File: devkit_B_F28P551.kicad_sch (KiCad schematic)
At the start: 4 parts, among them J1 DEVKIT_C2000_ROW_A, J2 DEVKIT_C2000_ROW_B, J3 JTAG_CTBP_10, U1 TMS320F28P551SG5PM

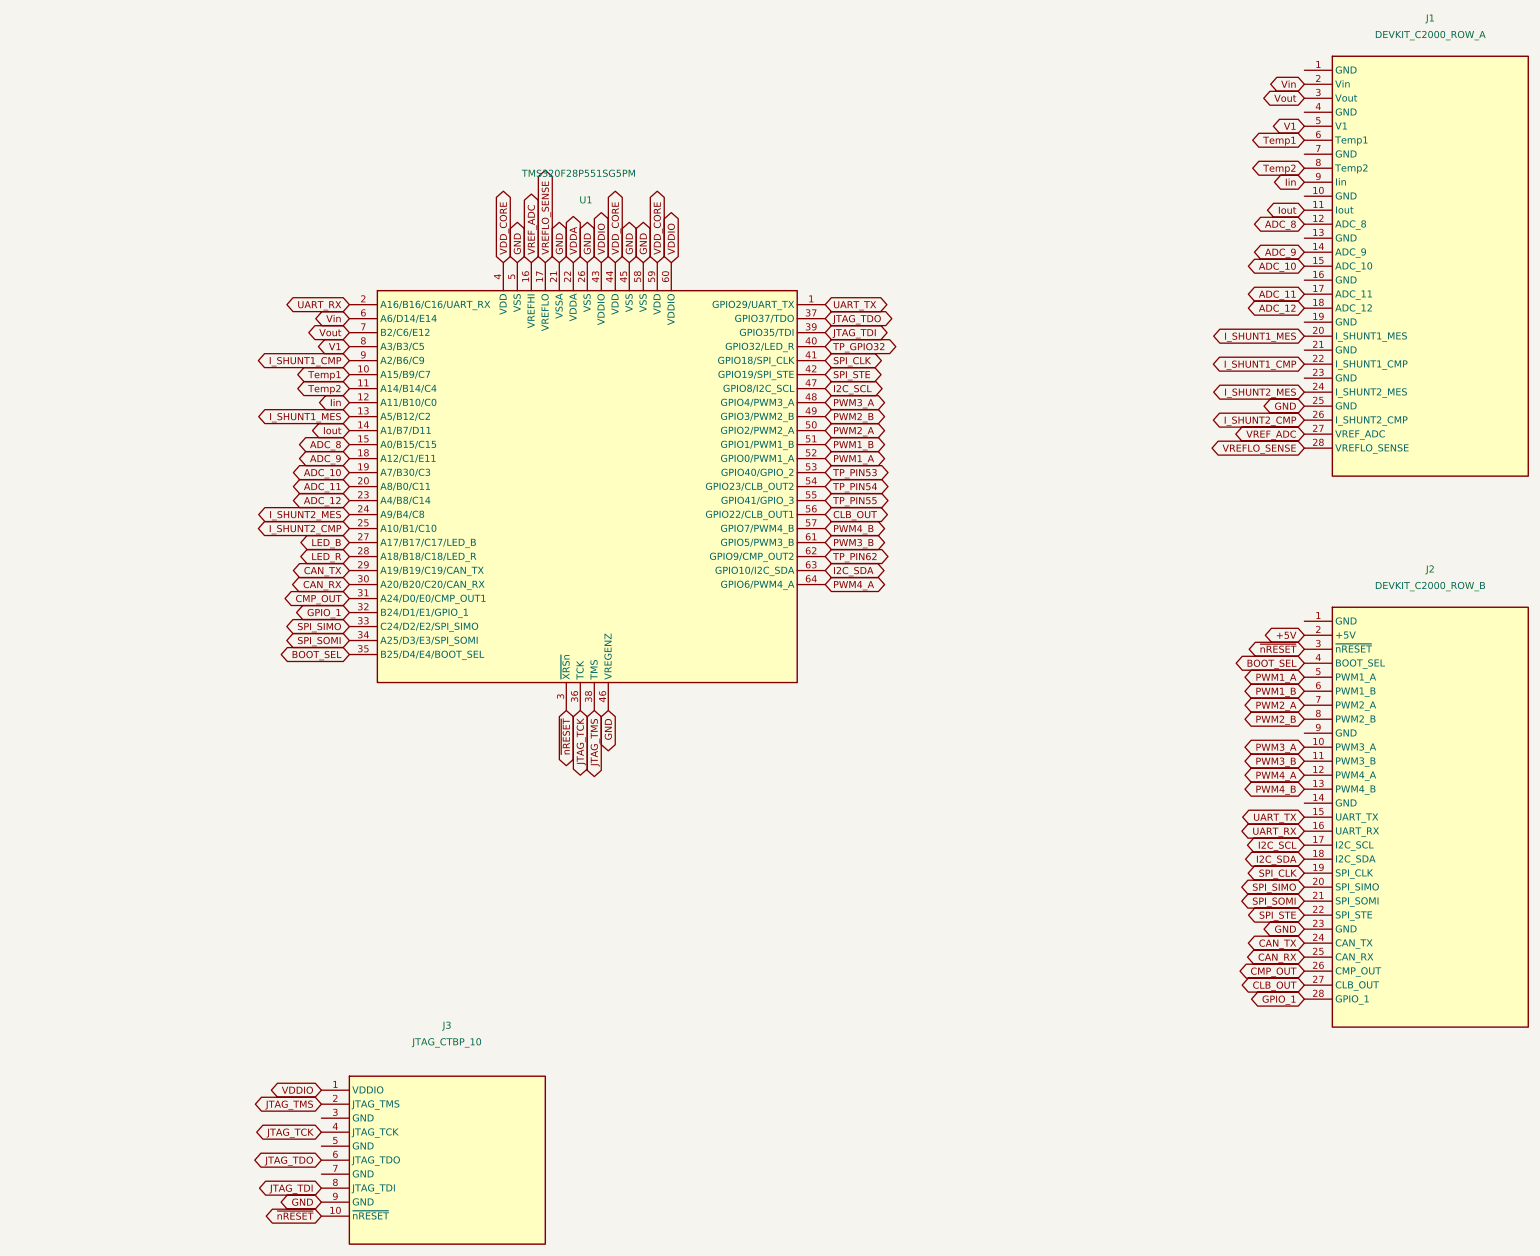
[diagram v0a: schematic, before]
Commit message: Symboles MCU en carre LQFP-64, 16 broches par cote de 1 a 64
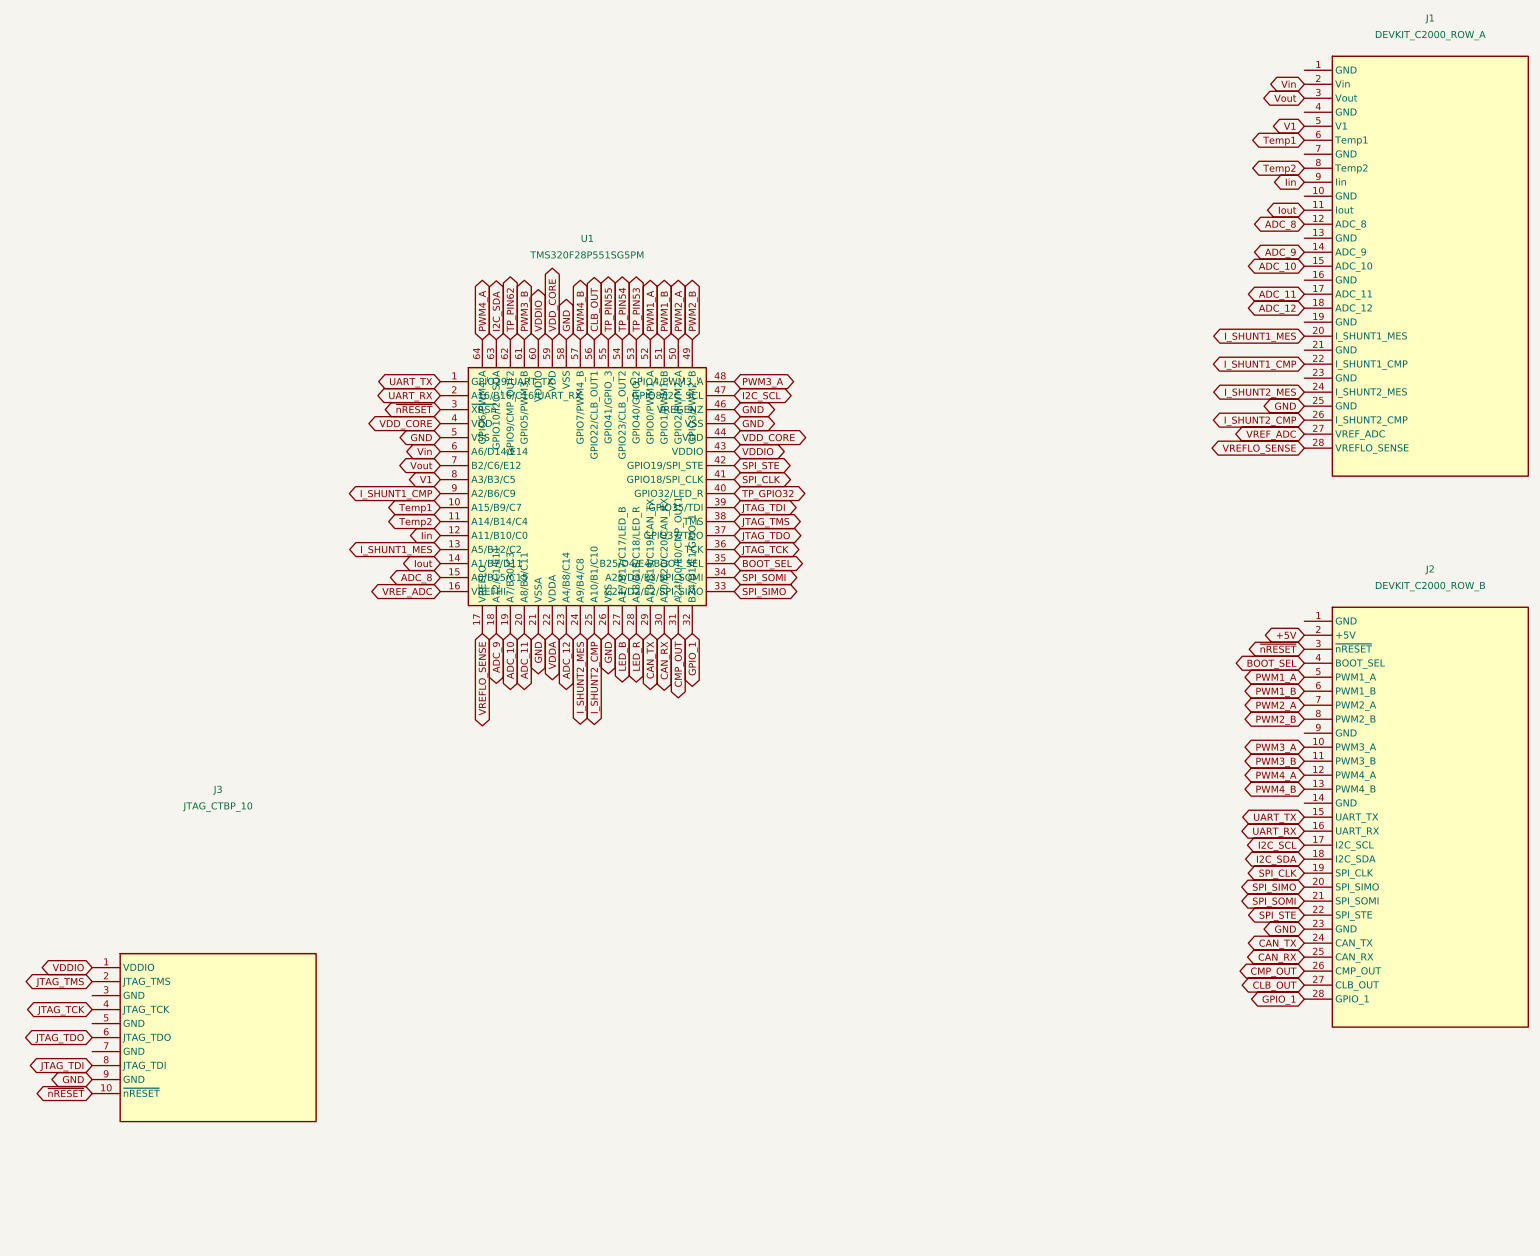
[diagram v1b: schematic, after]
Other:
- moved on the sheet: J3
